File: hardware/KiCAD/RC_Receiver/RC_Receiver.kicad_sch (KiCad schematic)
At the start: 7 parts, among them U1 NRF24L01_Breakout

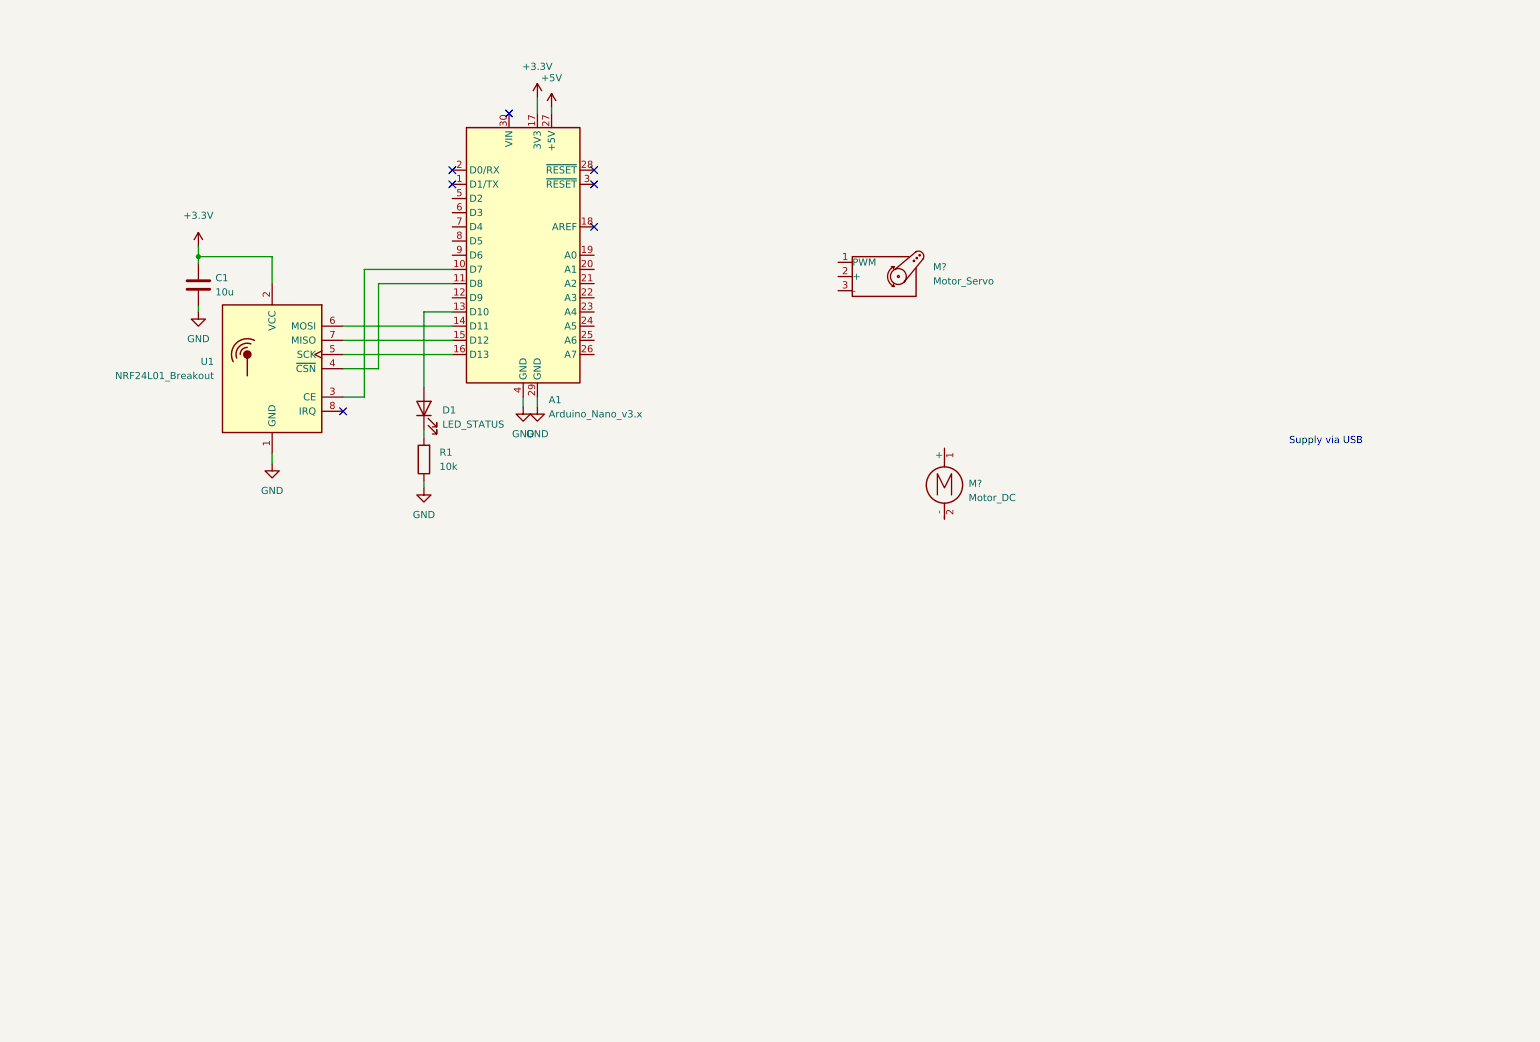
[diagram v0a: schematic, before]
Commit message: add schematic net names like described in the readme
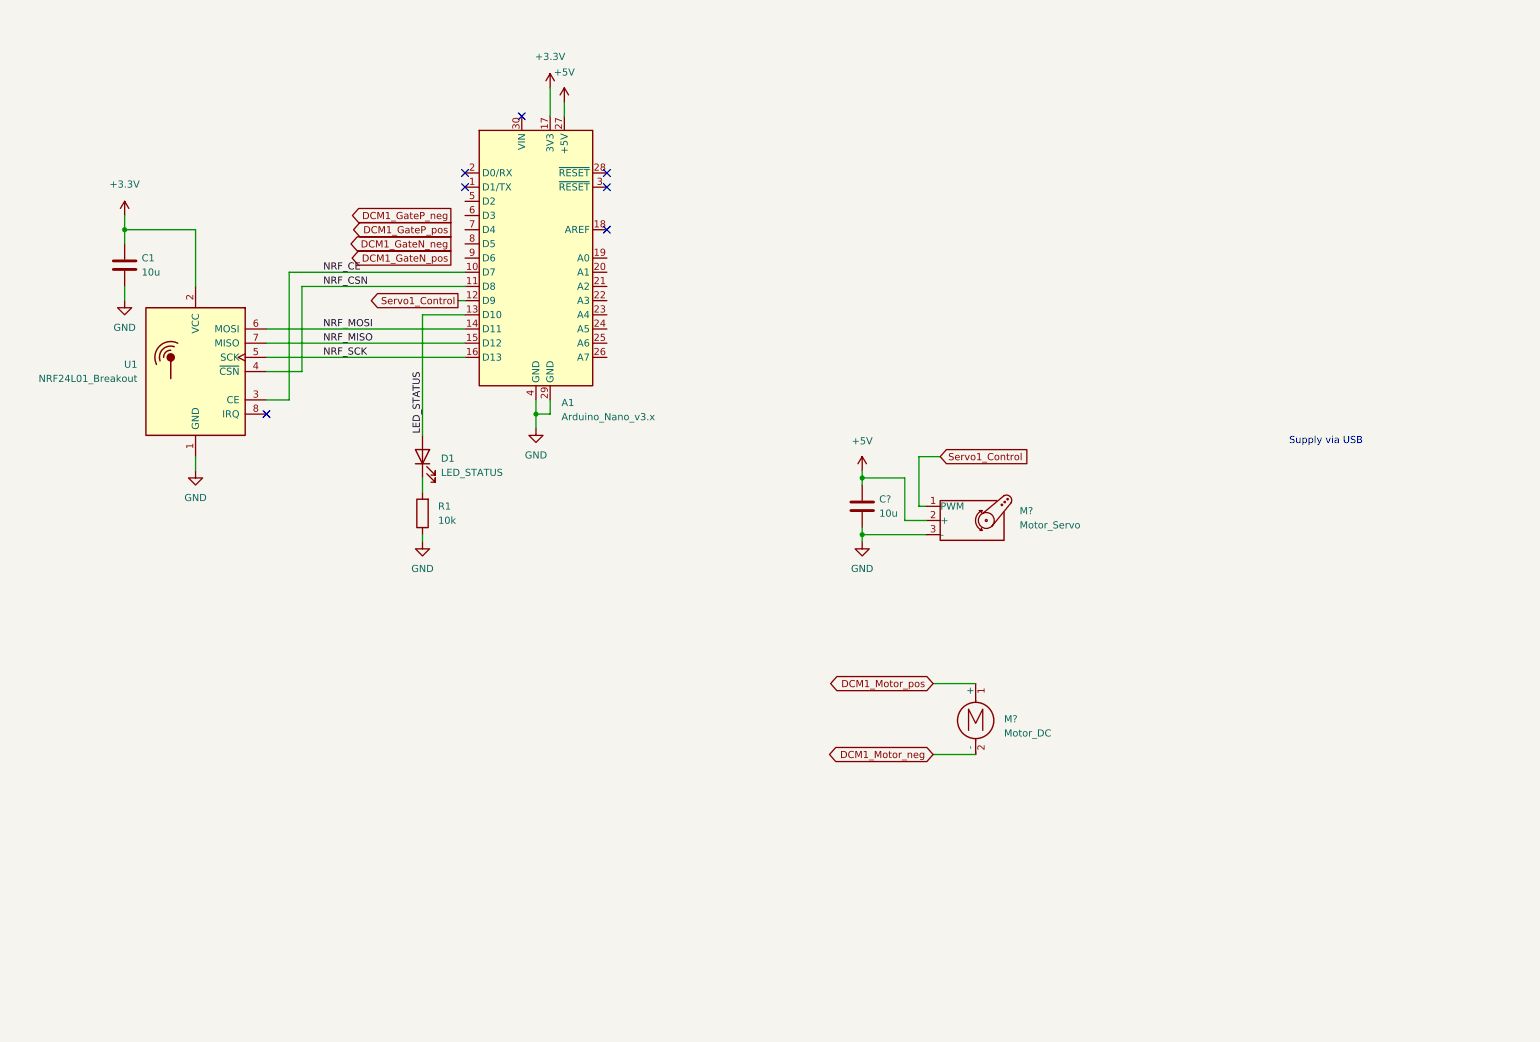
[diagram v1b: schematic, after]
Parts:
- removed M?: Motor_Servo, symbol Motor:Motor_Servo
- removed M?: Motor_DC, symbol Motor:Motor_DC
- added C?: 10u, symbol Device:C
- added M?: Motor_DC, symbol Motor:Motor_DC
- added M?: Motor_Servo, symbol Motor:Motor_Servo
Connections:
- net +5V: now also C?.1, M?.2 (+)
- net GND: now also C?.2, M?.3 (-)
- net NRF_CE: now reaches A1.10 (D7), U1.3 (CE)
- net NRF_CSN: now reaches A1.11 (D8), U1.4 (~{CSN})
- net NRF_SCK: now reaches A1.16 (D13), U1.5 (SCK)
- net NRF_MOSI: now reaches A1.14 (D11), U1.6 (MOSI)
- net NRF_MISO: now reaches A1.15 (D12), U1.7 (MISO)
- net LED_STATUS: now reaches A1.13 (D10), D1.2 (A)
- net Servo1_Control: now reaches A1.12 (D9)
- net Servo1_Control: now also M?.1 (PWM)
- new net DCM1_Motor_neg: M?.2 (-)
- new net DCM1_Motor_pos: M?.1 (+)
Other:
- moved on the sheet: A1, C1, D1, R1, U1

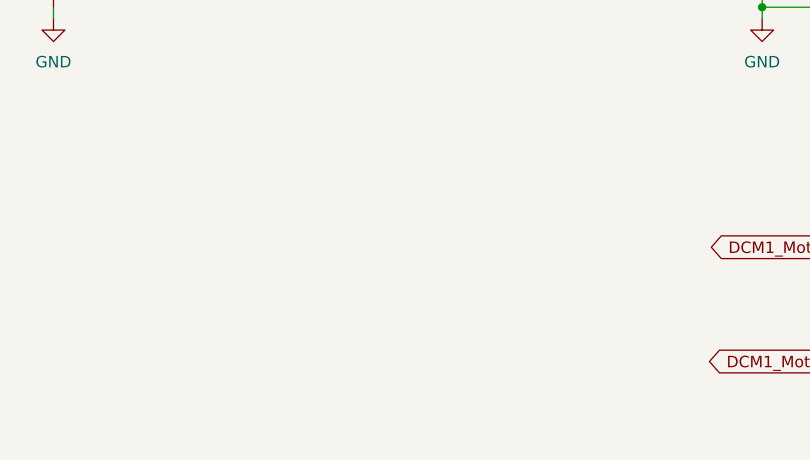
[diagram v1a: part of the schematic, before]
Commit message: add motor driver H-bridge
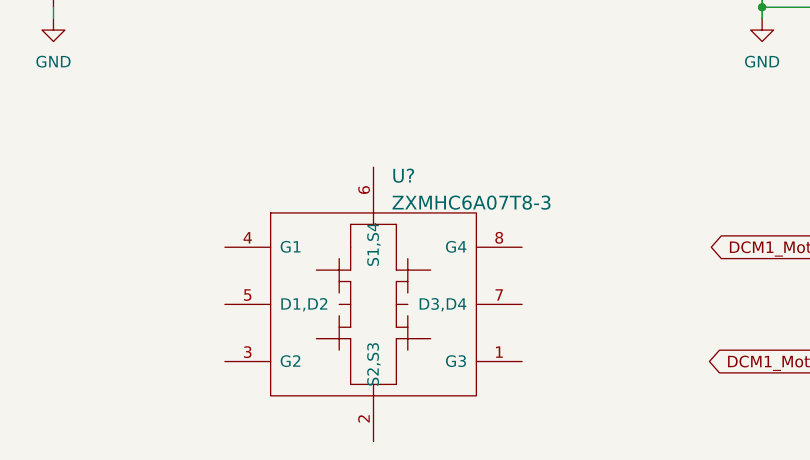
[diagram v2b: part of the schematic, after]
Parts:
- added U?: ZXMHC6A07T8-3, symbol redLabs:ZXMHC6A07T8-3
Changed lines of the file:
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@@
     (pin "1")
+  )
+  (symbol (lib_id "redLabs:ZXMHC6A07T8-3") (at 121.92 140.97 0) (unit 1)
+    (in_bom yes) (on_board yes) (fields_autoplaced)
+    (property "Reference" "U?" (id 0) (at 123.9394 126.7259 0)
+      (effects (font (size 1.524 1.524)) (justify left))
+    )
+    (property "Value" "ZXMHC6A07T8-3" (id 1) (at 123.9394 129.7193 0)
+      (effects (font (size 1.524 1.524)) (justify left))
+    )
+    (property "Footprint" "" (id 2) (at 121.92 140.97 0)
+      (effects (font (size 1.524 1.524)))
+    )
+    (property "Datasheet" "" (id 3) (at 121.92 140.97 0)
+      (effects (font (size 1.524 1.524)))
+    )
+    (pin "1")
+    (pin "2")
+    (pin "3")
+    (pin "4")
+    (pin "5")
+    (pin "6")
+    (pin "7")
+    (pin "8")
   )
   (symbol (lib_id "Device:R") (at 86.36 104.14 180) (unit 1)
@@
       (reference "U1") (unit 1) (value "NRF24L01_Breakout") (footprint "RF_Module:nRF24L01_Breakout")
     )
-  )
+    (path "/5f48357f-c353-4808-811f-74ed7ffaa7c6"
+      (reference "U?") (unit 1) (value "ZXMHC6A07T8-3") (footprint "")
+    )
+  )

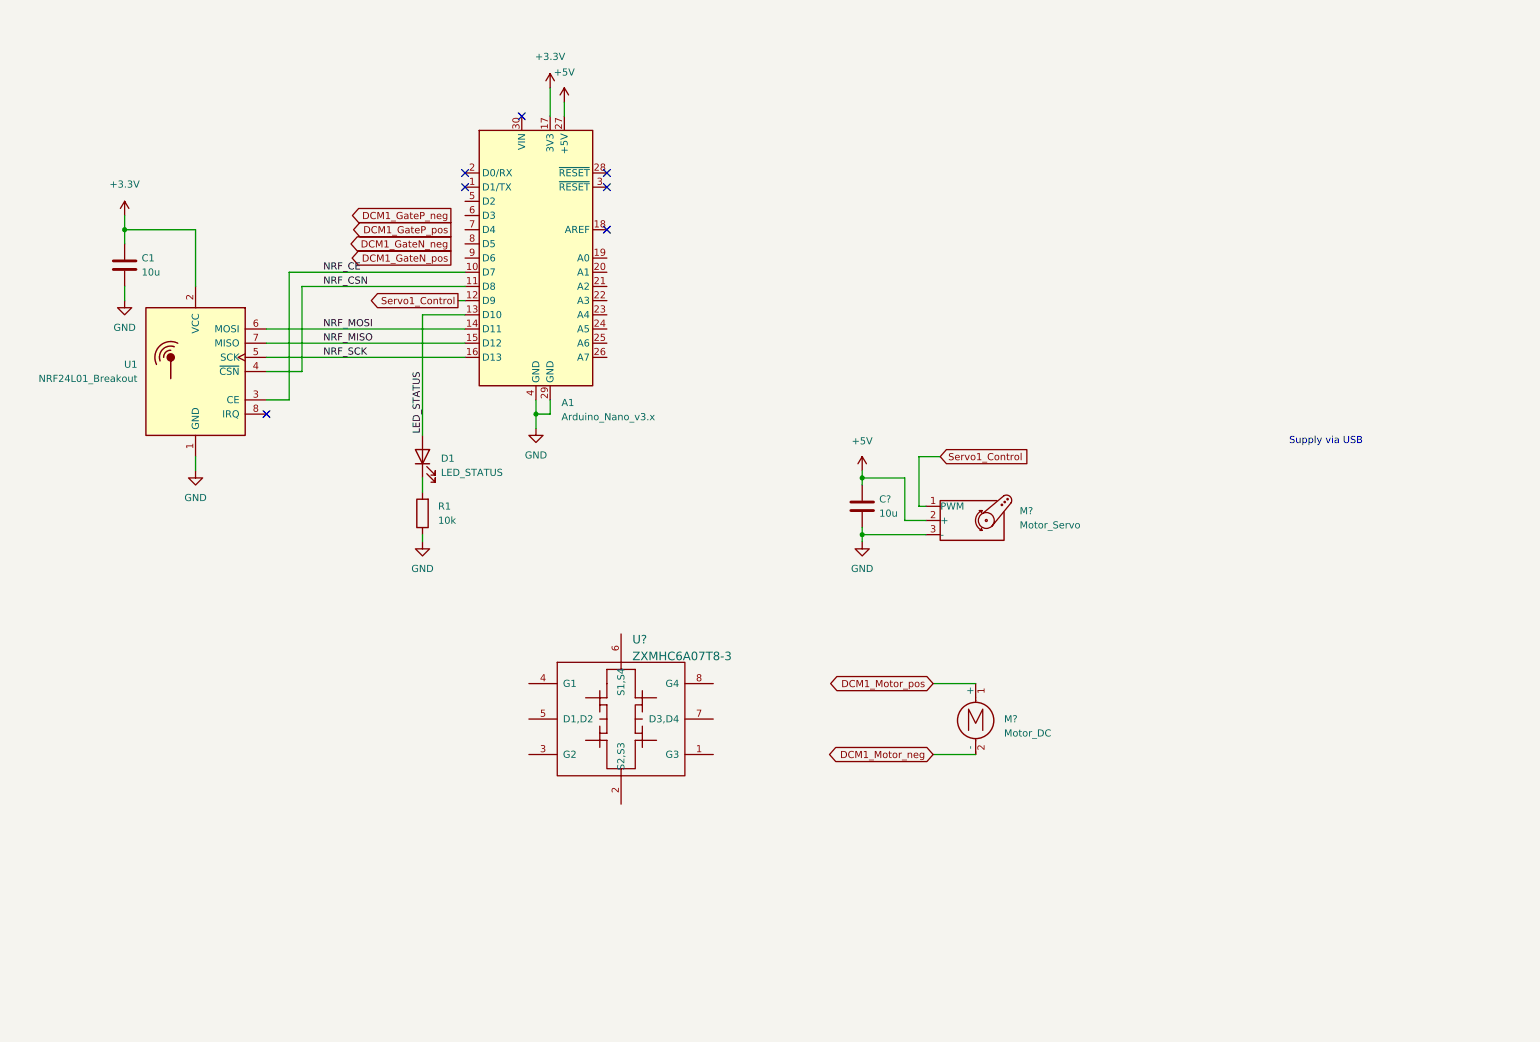
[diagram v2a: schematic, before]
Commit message: * add h-bridge driver
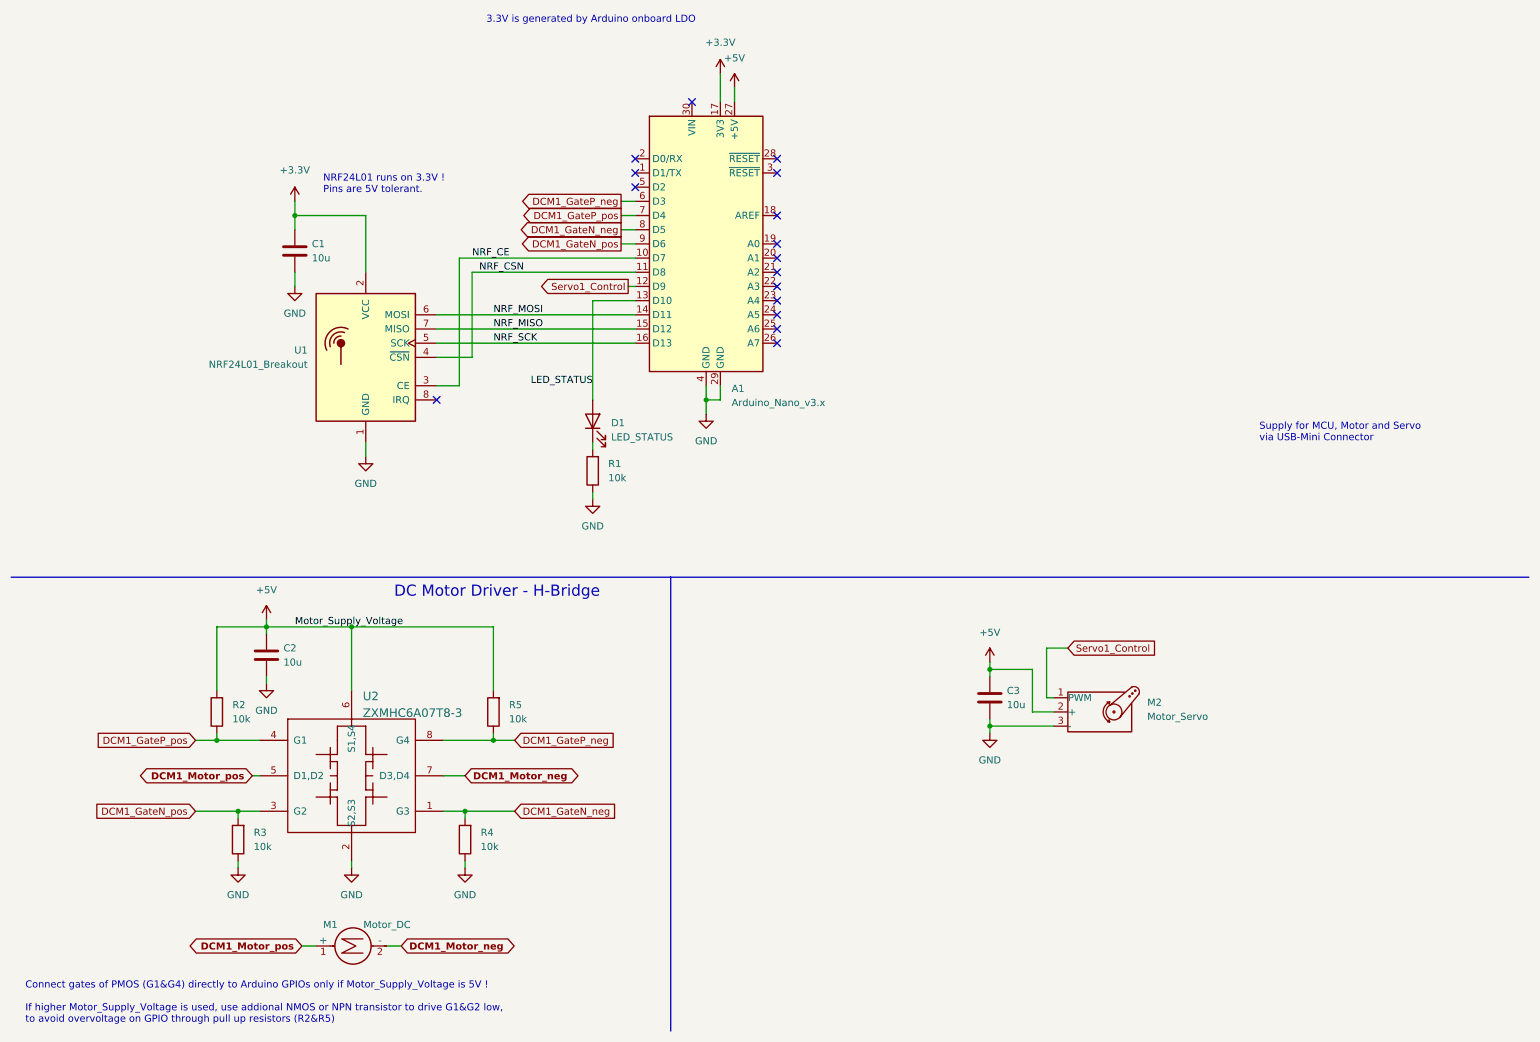
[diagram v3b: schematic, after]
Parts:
- added C2: 10u, symbol Device:C
- added R2, R3, R4, R5: 10k, symbol Device:R
- gave numbers to parts that had none: 4
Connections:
- net +5V: now also U2.6 (S1,S4), C2.1, R2.2, R5.2
- net DCM1_GateN_neg: now also A1.8 (D5), U2.1 (G3), R4.2
- net DCM1_GateN_pos: now also A1.9 (D6), U2.3 (G2), R3.2
- net DCM1_GateP_neg: now also A1.6 (D3), U2.8 (G4), R5.1
- net DCM1_GateP_pos: now also A1.7 (D4), U2.4 (G1), R2.1
- net DCM1_Motor_neg: now also U2.7 (D3,D4)
- net DCM1_Motor_pos: now also U2.5 (D1,D2)
- net GND: now also U2.2 (S2,S3), C2.2, R3.1, R4.1
- no-connect marks 7 -> 16
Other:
- note added: "3.3V is generated by Arduino onboard LDO"
- note added: "Connect gates of PMOS (G1&G4) directly to Arduino GPIOs only if Motor_Supply_Voltage is 5V ! If higher Motor_Supply_Voltage is used, use addional NMOS or NPN transistor to drive G1&G2 low, to avoid overvoltage on GPIO through pull up resistors (R2&R5)"
- note added: "DC Motor Driver - H-Bridge"
- note added: "NRF24L01 runs on 3.3V ! Pins are 5V tolerant."
- note added: "Supply for MCU, Motor and Servo via USB-Mini Connector"
- note removed: "Supply via USB"
- moved on the sheet: A1, C1, C3, D1, M1, M2, R1, U1, U2

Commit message: change value of series resistor for status LED
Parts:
- R1: value 10k -> 4k7
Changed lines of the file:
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@@
       (effects (font (size 1.27 1.27)) (justify right))
     )
-    (property "Value" "10k" (id 1) (at 119.634 97.7899 0)
+    (property "Value" "4k7" (id 1) (at 119.634 97.7899 0)
       (effects (font (size 1.27 1.27)) (justify right))
     )
@@
     )
     (path "/710c87df-58cf-4d1c-ad64-932a210b6aae"
-      (reference "R1") (unit 1) (value "10k") (footprint "")
+      (reference "R1") (unit 1) (value "4k7") (footprint "")
     )
     (path "/75202622-1795-44f1-83e8-a3062aaae217"
